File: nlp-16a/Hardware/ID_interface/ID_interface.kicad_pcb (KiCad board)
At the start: 2 copper layers, 209.6 x 154.9 mm, 79 parts, among them J1 Screw_Terminal_01x02, J10 Conn_02x10_Odd_Even, J11 Conn_02x10_Odd_Even, J2 Conn_02x10_Counter_Clockwise, J3 Conn_02x10_Odd_Even, J4 Conn_02x10_Odd_Even, J5 Screw_Terminal_01x02, J6 Screw_Terminal_01x02, J7 Screw_Terminal_01x02, J8 Screw_Terminal_01x02, J9 Conn_02x10_Odd_Even, U1 CD74HC00, U10 CD74HC00, U11 CD74HC00, U12 CD74HC00, U13 CD74HC00, U14 CD74HC00, U15 CD74HC00, U16 CD74HC00, U17 CD74HC00, U18 CD74HC00, U19 CD74HC00, U2 CD74HC00, U20 CD74HC00, U21 CD74HC00, U22 CD74HC00, U23 CD74HC00, U24 CD74HC00, U25 CD74HC00, U26 CD74HC00, U3 CD74HC00, U4 CD74HC00, U5 CD74HC00, U6 CD74HC00, U7 CD74HC00, U8 CD74HC00, U9 CD74HC00

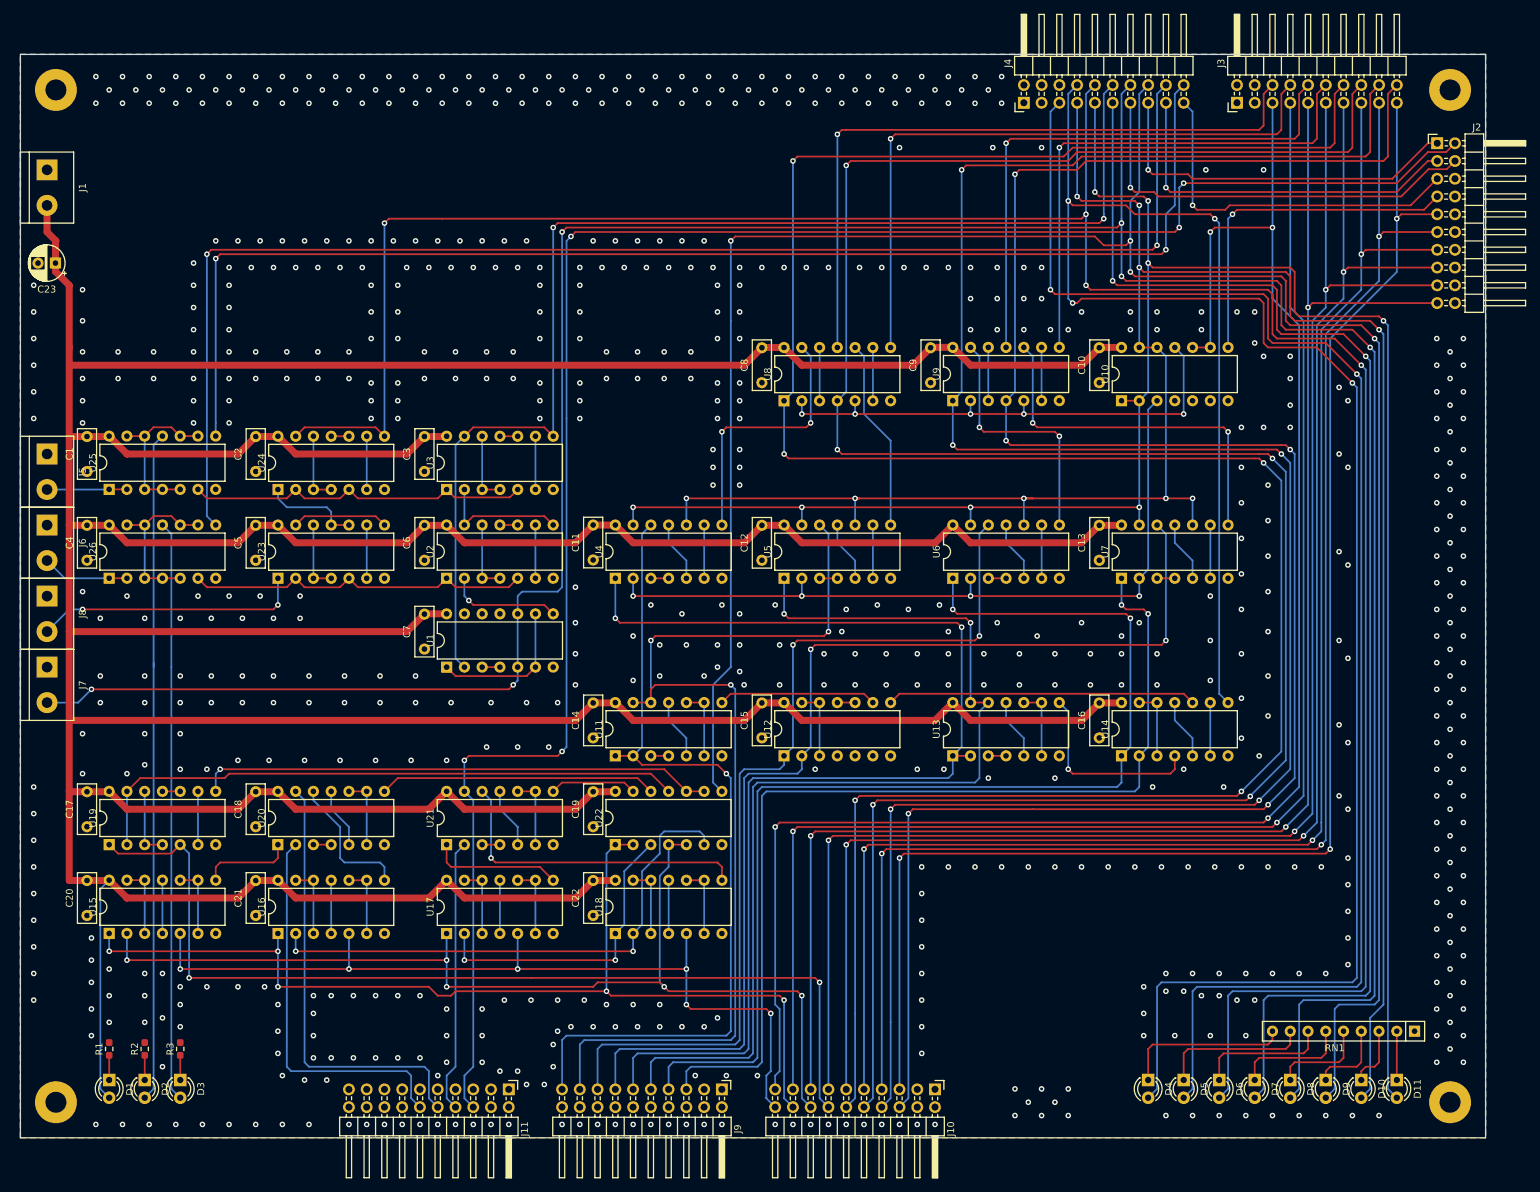
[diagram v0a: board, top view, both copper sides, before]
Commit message: 軽微な修正を加えてガーバー作成 発注
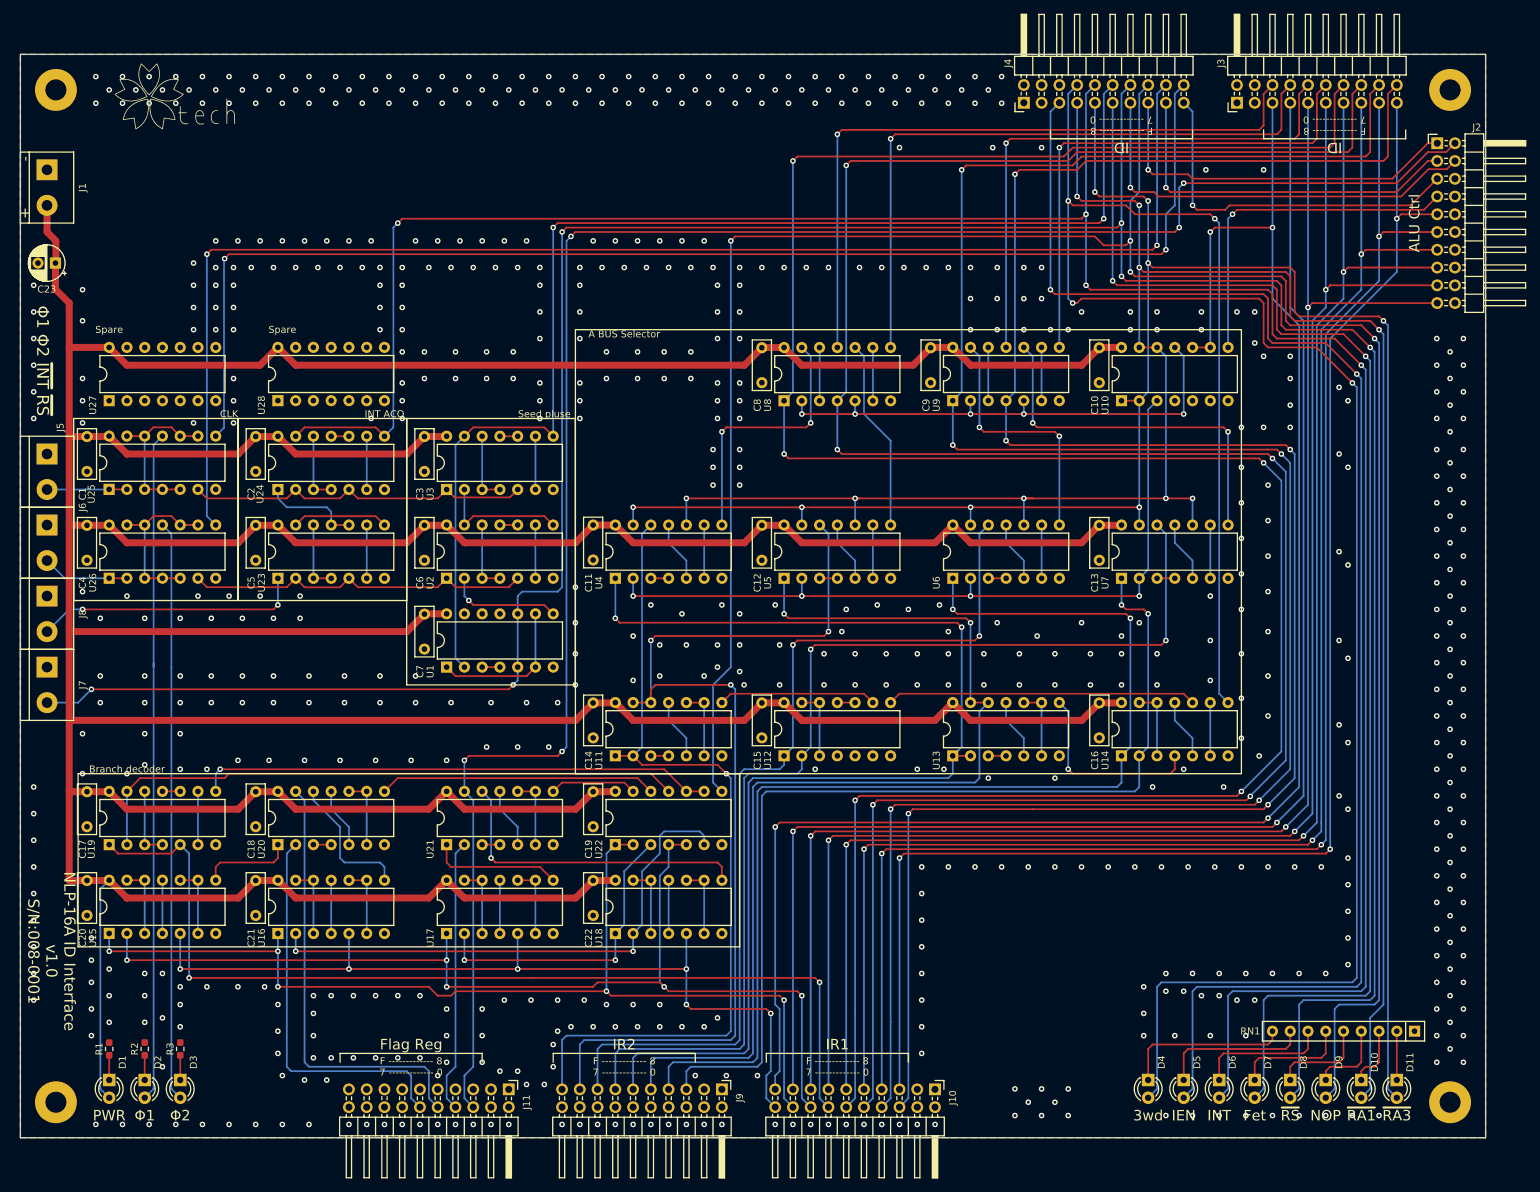
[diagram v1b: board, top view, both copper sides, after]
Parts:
- added G***: LOGO, LOGO, F.Cu at (53.3, 43.8)
- added U27: CD74HC00, Package_DIP:DIP-14_W7.62mm, F.Cu at (43.2, 87.0)
- added U28: CD74HC00, Package_DIP:DIP-14_W7.62mm, F.Cu at (67.3, 87.0)
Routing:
- net VCC: track 889.1 -> 892.1 mm
- net INT: track 346.2 -> 345.1 mm
- net phi1_1: track 186.4 -> 185.7 mm
- net GND: vias 704 -> 690
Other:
- board text added: "+ -"
- board text added: "3wd"
- board text added: "A BUS Selector"
- board text added: "ALU Ctrl"
- board text added: "Branch decoder"
- board text added: "CLK"
- board text added: "F ------------- 8 7 ------------- 0"
- board text added: "Fet"
- board text added: "Flag Reg"
- board text added: "ID"
- board text added: "IEN"
- board text added: "INT"
- board text added: "INT ACQ"
- board text added: "IR1"
- board text added: "IR2"
- board text added: "NLP-16A ID Interface v1.0 S/N:008-0001"
- board text added: "NOP"
- board text added: "PWR"
- board text added: "Seed pluse"
- board text added: "Spare"
- board text added: "~{RA1}"
- board text added: "~{RA3}"
- board text added: "~{RS}"
- board text added: "Φ1"
- board text added: "Φ1 Φ2 ~{INT} ~{RS}"
- board text added: "Φ2"

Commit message: v1.1全ガーバーを更新
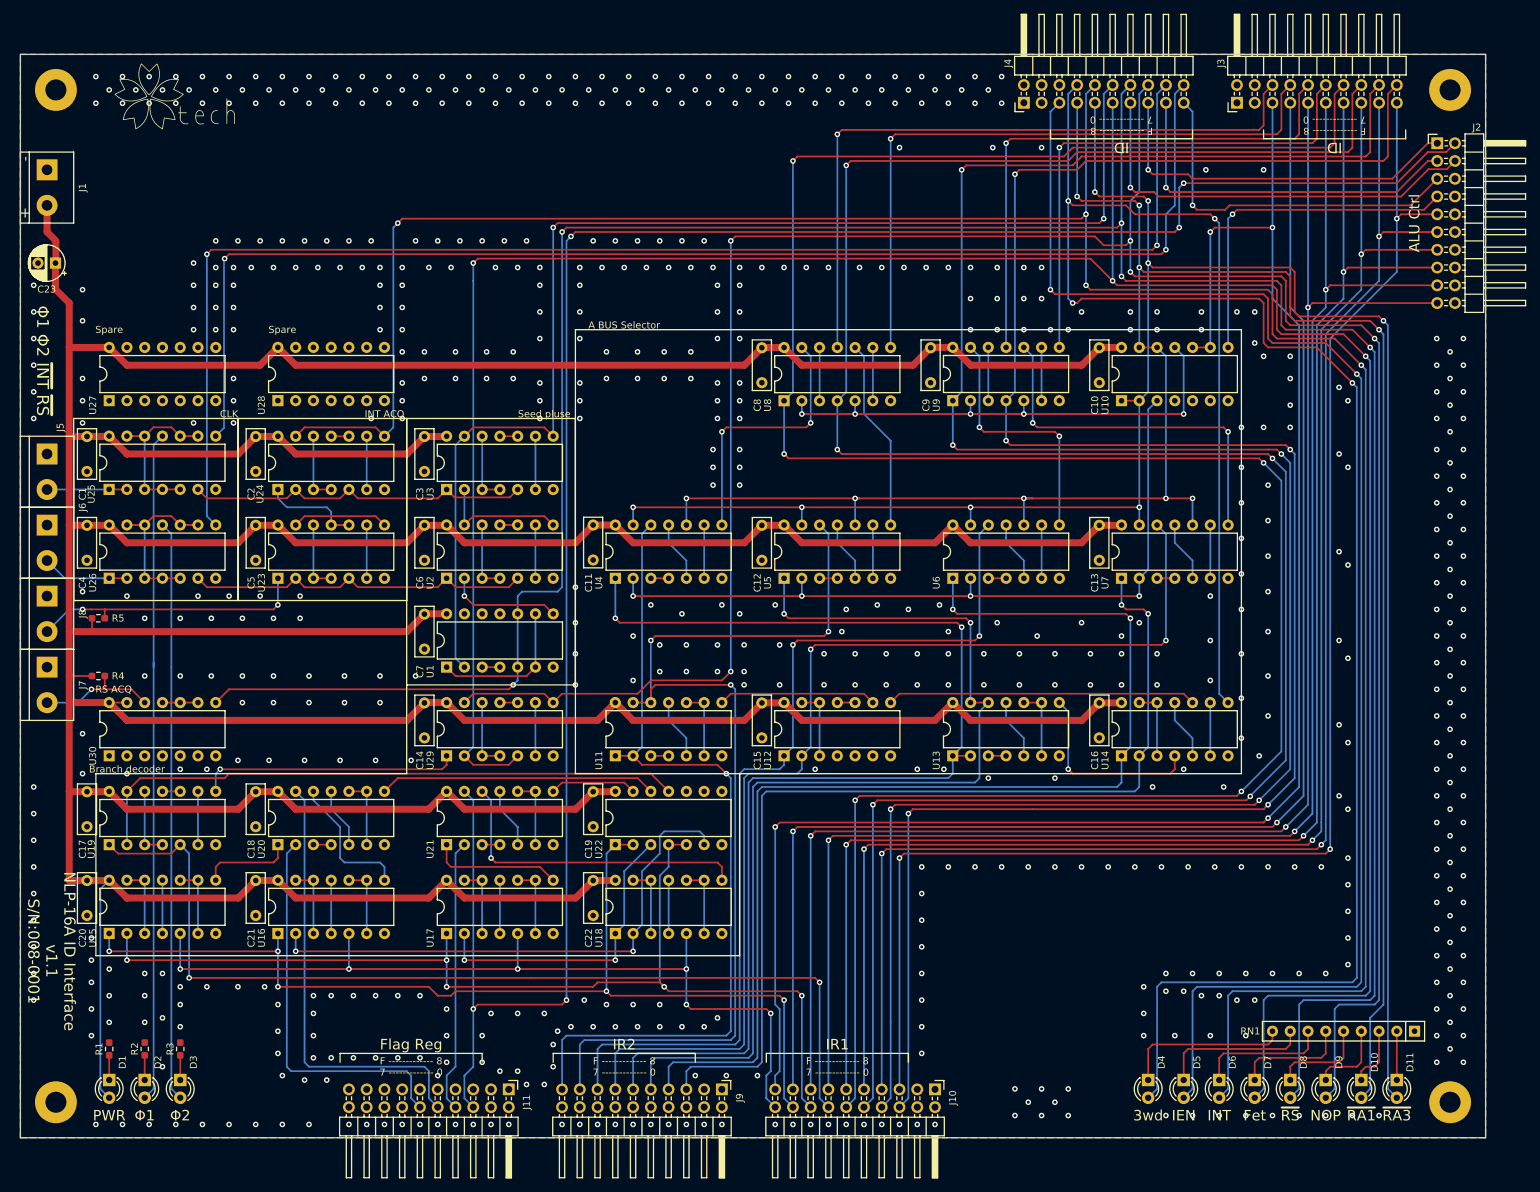
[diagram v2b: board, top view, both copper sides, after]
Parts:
- added R4: R, Resistor_SMD:R_0603_1608Metric_Pad0.98x0.95mm_HandSolder, F.Cu at (41.6, 126.4)
- added R5: R, Resistor_SMD:R_0603_1608Metric_Pad0.98x0.95mm_HandSolder, F.Cu at (41.6, 118.1)
- added U29: CD74HC00, Package_DIP:DIP-14_W7.62mm, F.Cu at (91.4, 137.8)
- added U30: CD74HC00, Package_DIP:DIP-14_W7.62mm, F.Cu at (43.2, 137.8)
- moved C14 24.1 mm to (88.3, 135.2)
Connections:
- net ~{Fetch_Status} renamed Fetch_Status
- J7 pad 2: ~{RS} -> ~{RS_INPUT}
- U22 pad 10: Net-(U19-Pad8) -> GND
- U22 pad 8: NOP -> unconnected-(U22-Pad8)
- U22 pad 9: Net-(U19-Pad8) -> GND
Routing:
- net Fetch_Status: track 190.8 -> 363.5 mm, vias 2 -> 3
- net Net-(U19-Pad8): track 74.0 -> 37.4 mm
- net Flag_C: track 275.2 -> 305.4 mm
- net ~{RS}: track 408.1 -> 383.9 mm, vias 6 -> 5
- net NOP: track 323.5 -> 345.8 mm, vias 4 -> 5
- net ~{RS_INPUT}: track 0.00 -> 17.4 mm, vias 0 -> 1
- net VCC: track 892.1 -> 902.9 mm
- net Net-(U29-Pad12): track 0.00 -> 10.2 mm
- net Net-(U29-Pad6): track 0.00 -> 7.62 mm
- net Net-(U30-Pad10): track 0.00 -> 5.08 mm
- net Net-(U29-Pad10): track 0.00 -> 2.54 mm
- net ~{INT_INPUT}: track 38.4 -> 39.7 mm
- net GND: vias 690 -> 670
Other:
- board text added: "NLP-16A ID Interface v1.1 S/N:008-0001"
- board text added: "RS ACQ"
- board text removed: "NLP-16A ID Interface v1.0 S/N:008-0001"
